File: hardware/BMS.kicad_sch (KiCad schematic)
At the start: 6 parts

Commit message: finished schematic except for 12v buck boost
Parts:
- added C69: 0.22u, Capacitor_SMD:C_0603_1608Metric_Pad1.08x0.95mm_HandSolder, symbol Device:C_Small
- added C70: 0.1u, Capacitor_SMD:C_0603_1608Metric_Pad1.08x0.95mm_HandSolder, symbol Device:C_Small
- added C71, C72, C73, C74, C75, C76: 100pF, Capacitor_SMD:C_0603_1608Metric_Pad1.08x0.95mm_HandSolder, symbol Device:C_Small
- added R107: 100k, Resistor_SMD:R_0603_1608Metric_Pad0.98x0.95mm_HandSolder, symbol Device:R_Small
- added R108: 10, Resistor_SMD:R_0603_1608Metric_Pad0.98x0.95mm_HandSolder, symbol Device:R_Small
- added R109, R110: 1k, Resistor_SMD:R_0603_1608Metric_Pad0.98x0.95mm_HandSolder, symbol Device:R_Small
- added R111, R112, R113, R114: 51, Resistor_SMD:R_0603_1608Metric_Pad0.98x0.95mm_HandSolder, symbol Device:R_Small
- added TR1, TR2: ADTT3-2, RF_Mini-Circuits:Mini-Circuits_CD636_H4.11mm, symbol Transformer:ADTT3-2
- added U13, U14: PESD5V0L2BT, LHRS_ICs:SOT23_NXP, symbol lhrs_misc:PESD5V0L2BT
- C67: renamed from C?; footprint (none) -> Capacitor_SMD:C_0603_1608Metric_Pad1.08x0.95mm_HandSolder
- C68: renamed from C?; value 0.1u -> 0.22u; footprint (none) -> Capacitor_SMD:C_0603_1608Metric_Pad1.08x0.95mm_HandSolder
- IC4: renamed from IC?; footprint SOP65P640X120-16N -> LHRS_ICs:SOP65P640X120-16N
- R104, R105, R106: renamed from R?; footprint (none) -> Resistor_SMD:R_0603_1608Metric_Pad0.98x0.95mm_HandSolder
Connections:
- net GND: now also C68.2, IC4.6 (SCLK), IC4.7 (NCS), IC4.8 (NUART/SPI_(SPI_RDY)), C69.2, C70.2, C71.2, C72.2, C73.2, C74.2, C75.1, C76.1, R107.2, U13.3, U14.3
- net INH: now also IC4.16 (INH), R107.1
- net at IC4.1 (DVDD): now also C68.1
- net COMLP: now reaches IC4.10 (COMLP)
- net COMLP: now also C71.1, R109.1, R111.1
- net COMLN: now reaches IC4.11 (COMLN)
- net COMLN: now also C72.1, R109.2, R112.1
- net COMHN: now reaches IC4.12 (COMHN)
- net COMHN: now also C74.1, R110.2, R114.1
- net COMHP: now reaches IC4.13 (COMHP)
- net COMHP: now also C73.1, R110.1, R113.1
- net at IC4.14 (CVDD): now also C69.1
- net at IC4.15 (BAT): now also C70.1, R108.1
- new net: C75.2, TR1.2
- new net: R111.2, TR2.3, U14.2
- new net: R114.2, TR1.1, U13.1
- new net: R113.2, TR1.3, U13.2
- new net: R112.2, TR2.1, U14.1
- new net: C76.2, TR2.2
- new net VBAT: R108.2
- new net isolatedCOMHN: TR1.6
- new net isolatedCOMHP: TR1.4
- new net isolatedCOMLN: TR2.6
- new net isolatedCOMLP: TR2.4
- no-connect marks 0 -> 2
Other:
- note added: "General Isolation"
- note added: "Transformer Isolation"
- moved on the sheet: C68, IC4

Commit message: added 12V buck boost
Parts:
- renumbered C67 to C68, C68 to C69, C69 to C70, C70 to C71, C71 to C72, C72 to C73, C73 to C74, C74 to C75, C75 to C76, C76 to C77, R104 to R108, R105 to R109, R106 to R110, R107 to R111, R108 to R112, R109 to R113, R110 to R114, R111 to R115, R112 to R116, R113 to R117, R114 to R118
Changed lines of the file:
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@@
 		(in_pos_files yes)
 		(dnp no)
-		(property "Reference" "C75"
+		(property "Reference" "C76"
 			(at 228.727 88.519 90)
 			(show_name no)
@@
 			(project "PS-BPSLeader"
 				(path "/d4a4ed4f-0983-4aef-b212-0e3284ab3963/e693f766-4bc7-4d67-a672-39e10f482b8b"
-					(reference "C75")
+					(reference "C76")
 					(unit 1)
 				)
@@
 		(dnp no)
 		(fields_autoplaced yes)
-		(property "Reference" "C67"
+		(property "Reference" "C68"
 			(at 22.86 27.9462 0)
 			(show_name no)
@@
 			(project "PS-BPSLeader"
 				(path "/d4a4ed4f-0983-4aef-b212-0e3284ab3963/e693f766-4bc7-4d67-a672-39e10f482b8b"
-					(reference "C67")
+					(reference "C68")
 					(unit 1)
 				)
@@
 		(dnp no)
 		(fields_autoplaced yes)
-		(property "Reference" "R111"
+		(property "Reference" "R115"
 			(at 189.23 118.11 90)
 			(show_name no)
@@
 			(project "PS-BPSLeader"
 				(path "/d4a4ed4f-0983-4aef-b212-0e3284ab3963/e693f766-4bc7-4d67-a672-39e10f482b8b"
-					(reference "R111")
+					(reference "R115")
 					(unit 1)
 				)
@@
 		(dnp no)
 		(fields_autoplaced yes)
-		(property "Reference" "R104"
+		(property "Reference" "R108"
 			(at 41.275 26.0349 0)
 			(show_name no)
@@
 			(project "PS-BPSLeader"
 				(path "/d4a4ed4f-0983-4aef-b212-0e3284ab3963/e693f766-4bc7-4d67-a672-39e10f482b8b"
-					(reference "R104")
+					(reference "R108")
 					(unit 1)
 				)
@@
 		(dnp no)
 		(fields_autoplaced yes)
-		(property "Reference" "C72"
+		(property "Reference" "C73"
 			(at 177.8 144.1512 0)
 			(show_name no)
@@
 			(project "PS-BPSLeader"
 				(path "/d4a4ed4f-0983-4aef-b212-0e3284ab3963/e693f766-4bc7-4d67-a672-39e10f482b8b"
-					(reference "C72")
+					(reference "C73")
 					(unit 1)
 				)
@@
 		(dnp no)
 		(fields_autoplaced yes)
-		(property "Reference" "C74"
+		(property "Reference" "C75"
 			(at 179.07 101.6062 0)
 			(show_name no)
@@
 			(project "PS-BPSLeader"
 				(path "/d4a4ed4f-0983-4aef-b212-0e3284ab3963/e693f766-4bc7-4d67-a672-39e10f482b8b"
-					(reference "C74")
+					(reference "C75")
 					(unit 1)
 				)
@@
 		(dnp no)
 		(fields_autoplaced yes)
-		(property "Reference" "R108"
+		(property "Reference" "R112"
 			(at 120.65 83.8199 0)
 			(show_name no)
@@
 			(project "PS-BPSLeader"
 				(path "/d4a4ed4f-0983-4aef-b212-0e3284ab3963/e693f766-4bc7-4d67-a672-39e10f482b8b"
-					(reference "R108")
+					(reference "R112")
 					(unit 1)
 				)
@@
 		(dnp no)
 		(fields_autoplaced yes)
-		(property "Reference" "C71"
+		(property "Reference" "C72"
 			(at 177.8 126.3712 0)
 			(show_name no)
@@
 			(project "PS-BPSLeader"
 				(path "/d4a4ed4f-0983-4aef-b212-0e3284ab3963/e693f766-4bc7-4d67-a672-39e10f482b8b"
-					(reference "C71")
+					(reference "C72")
 					(unit 1)
 				)
@@
 		(dnp no)
 		(fields_autoplaced yes)
-		(property "Reference" "C73"
+		(property "Reference" "C74"
 			(at 179.07 83.8262 0)
 			(show_name no)
@@
 			(project "PS-BPSLeader"
 				(path "/d4a4ed4f-0983-4aef-b212-0e3284ab3963/e693f766-4bc7-4d67-a672-39e10f482b8b"
-					(reference "C73")
+					(reference "C74")
 					(unit 1)
 				)
@@
 		(dnp no)
 		(fields_autoplaced yes)
-		(property "Reference" "R109"
+		(property "Reference" "R113"
 			(at 167.64 131.4449 0)
 			(show_name no)
@@
 			(project "PS-BPSLeader"
 				(path "/d4a4ed4f-0983-4aef-b212-0e3284ab3963/e693f766-4bc7-4d67-a672-39e10f482b8b"
-					(reference "R109")
+					(reference "R113")
 					(unit 1)
 				)
@@
 		(dnp no)
 		(fields_autoplaced yes)
-		(property "Reference" "C70"
+		(property "Reference" "C71"
 			(at 121.285 91.4462 0)
 			(show_name no)
@@
 			(project "PS-BPSLeader"
 				(path "/d4a4ed4f-0983-4aef-b212-0e3284ab3963/e693f766-4bc7-4d67-a672-39e10f482b8b"
-					(reference "C70")
+					(reference "C71")
 					(unit 1)
 				)
@@
 		(dnp no)
 		(fields_autoplaced yes)
-		(property "Reference" "R106"
+		(property "Reference" "R110"
 			(at 60.96 26.0349 0)
 			(show_name no)
@@
 			(project "PS-BPSLeader"
 				(path "/d4a4ed4f-0983-4aef-b212-0e3284ab3963/e693f766-4bc7-4d67-a672-39e10f482b8b"
-					(reference "R106")
+					(reference "R110")
 					(unit 1)
 				)
@@
 		(dnp no)
 		(fields_autoplaced yes)
-		(property "Reference" "R114"
+		(property "Reference" "R118"
 			(at 189.865 93.98 90)
 			(show_name no)
@@
 			(project "PS-BPSLeader"
 				(path "/d4a4ed4f-0983-4aef-b212-0e3284ab3963/e693f766-4bc7-4d67-a672-39e10f482b8b"
-					(reference "R114")
+					(reference "R118")
 					(unit 1)
 				)
@@
 		(in_pos_files yes)
 		(dnp no)
-		(property "Reference" "C76"
+		(property "Reference" "C77"
 			(at 229.362 131.064 90)
 			(show_name no)
@@
 			(project "PS-BPSLeader"
 				(path "/d4a4ed4f-0983-4aef-b212-0e3284ab3963/e693f766-4bc7-4d67-a672-39e10f482b8b"
-					(reference "C76")
+					(reference "C77")
 					(unit 1)
 				)
@@
 		(dnp no)
 		(fields_autoplaced yes)
-		(property "Reference" "R113"
+		(property "Reference" "R117"
 			(at 189.865 76.2 90)
 			(show_name no)
@@
 			(project "PS-BPSLeader"
 				(path "/d4a4ed4f-0983-4aef-b212-0e3284ab3963/e693f766-4bc7-4d67-a672-39e10f482b8b"
-					(reference "R113")
+					(reference "R117")
 					(unit 1)
 				)
@@
 		(dnp no)
 		(fields_autoplaced yes)
-		(property "Reference" "R110"
+		(property "Reference" "R114"
 			(at 168.275 88.8999 0)
 			(show_name no)
@@
 			(project "PS-BPSLeader"
 				(path "/d4a4ed4f-0983-4aef-b212-0e3284ab3963/e693f766-4bc7-4d67-a672-39e10f482b8b"
-					(reference "R110")
+					(reference "R114")
 					(unit 1)
 				)
@@
 		(dnp no)
 		(fields_autoplaced yes)
-		(property "Reference" "C68"
+		(property "Reference" "C69"
 			(at 47.625 114.9412 0)
 			(show_name no)
@@
 			(project "PS-BPSLeader"
 				(path "/d4a4ed4f-0983-4aef-b212-0e3284ab3963/e693f766-4bc7-4d67-a672-39e10f482b8b"
-					(reference "C68")
+					(reference "C69")
 					(unit 1)
 				)
@@
 		(dnp no)
 		(fields_autoplaced yes)
-		(property "Reference" "R107"
+		(property "Reference" "R111"
 			(at 80.645 25.3999 0)
 			(show_name no)
@@
 			(project "PS-BPSLeader"
 				(path "/d4a4ed4f-0983-4aef-b212-0e3284ab3963/e693f766-4bc7-4d67-a672-39e10f482b8b"
-					(reference "R107")
+					(reference "R111")
 					(unit 1)
 				)
@@
 		(dnp no)
 		(fields_autoplaced yes)
-		(property "Reference" "R112"
+		(property "Reference" "R116"
 			(at 189.23 135.89 90)
 			(show_name no)
@@
 			(project "PS-BPSLeader"
 				(path "/d4a4ed4f-0983-4aef-b212-0e3284ab3963/e693f766-4bc7-4d67-a672-39e10f482b8b"
-					(reference "R112")
+					(reference "R116")
 					(unit 1)
 				)
@@
 		(dnp no)
 		(fields_autoplaced yes)
-		(property "Reference" "C69"
+		(property "Reference" "C70"
 			(at 108.585 92.7162 0)
 			(show_name no)
@@
 			(project "PS-BPSLeader"
 				(path "/d4a4ed4f-0983-4aef-b212-0e3284ab3963/e693f766-4bc7-4d67-a672-39e10f482b8b"
-					(reference "C69")
+					(reference "C70")
 					(unit 1)
 				)
@@
 		(dnp no)
 		(fields_autoplaced yes)
-		(property "Reference" "R105"
+		(property "Reference" "R109"
 			(at 51.435 26.0349 0)
 			(show_name no)
@@
 			(project "PS-BPSLeader"
 				(path "/d4a4ed4f-0983-4aef-b212-0e3284ab3963/e693f766-4bc7-4d67-a672-39e10f482b8b"
-					(reference "R105")
-					(unit 1)
-				)
+					(reference "R109")
+					(unit 1)
+				)

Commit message: forgot to push last night
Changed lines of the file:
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@@
 	)
 	(hierarchical_label "MOSI{slash}RX"
-		(shape input)
+		(shape bidirectional)
 		(at 38.735 32.385 270)
 		(effects
@@
 	)
 	(hierarchical_label "MOSI{slash}RX"
-		(shape input)
+		(shape bidirectional)
 		(at 40.005 91.44 180)
 		(effects
@@
 	)
 	(hierarchical_label "MISO{slash}TX"
-		(shape input)
+		(shape bidirectional)
 		(at 48.895 32.385 270)
 		(effects

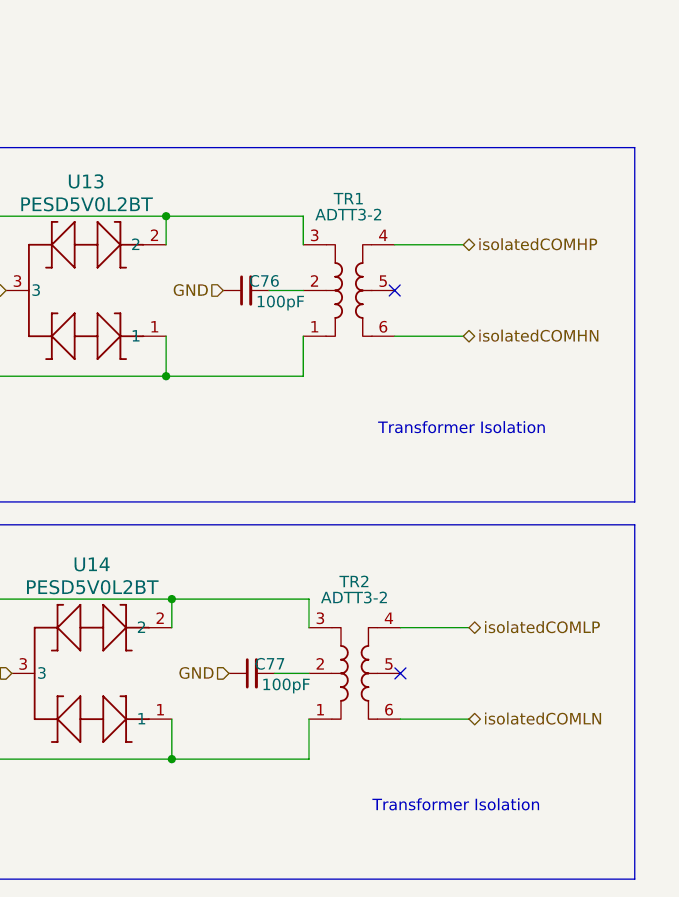
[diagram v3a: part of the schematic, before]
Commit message: kms drc crashed and didn't save layout
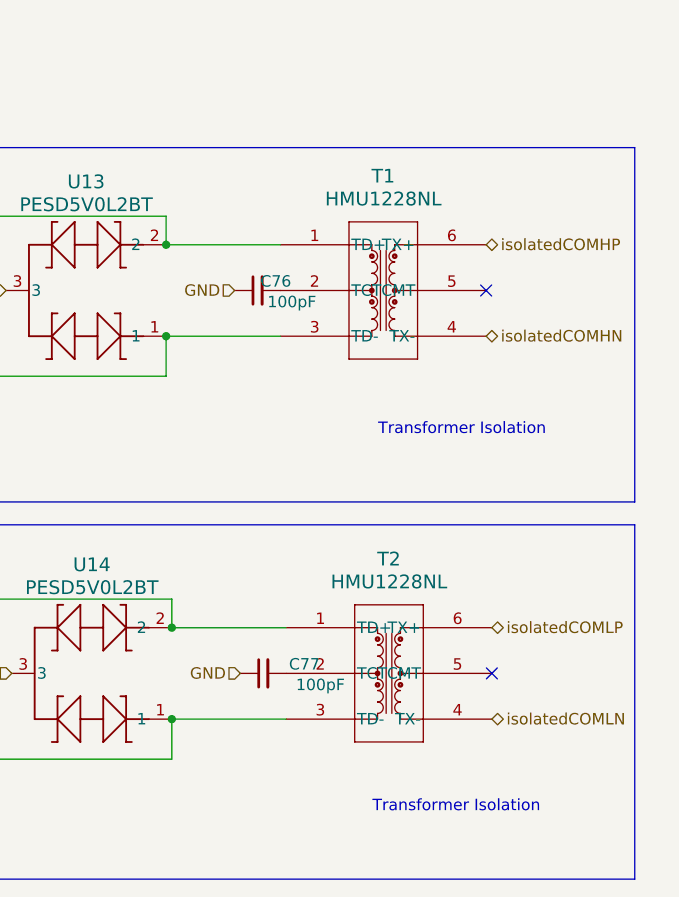
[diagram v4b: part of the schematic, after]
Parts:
- removed TR1, TR2: ADTT3-2, RF_Mini-Circuits:Mini-Circuits_CD636_H4.11mm, symbol Transformer:ADTT3-2
- added T1, T2: HMU1228NL, LHRS_Special:HMU1228NL_PUL, symbol lhrs_special:HMU1228NL
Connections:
- net isolatedCOMHN: now also T1.4 (TX-)
- net isolatedCOMHP: now also T1.6 (TX+)
- net isolatedCOMLN: now also T2.4 (TX-)
- net isolatedCOMLP: now also T2.6 (TX+)
- net at C76.2: now also T1.2 (TCT)
- net at R115.2, U14.2: now also T2.1 (TD+)
- net at R118.2, U13.1: now also T1.3 (TD-)
- net at R117.2, U13.2: now also T1.1 (TD+)
- net at R116.2, U14.1: now also T2.3 (TD-)
- net at C77.2: now also T2.2 (TCT)
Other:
- moved on the sheet: C76, C77

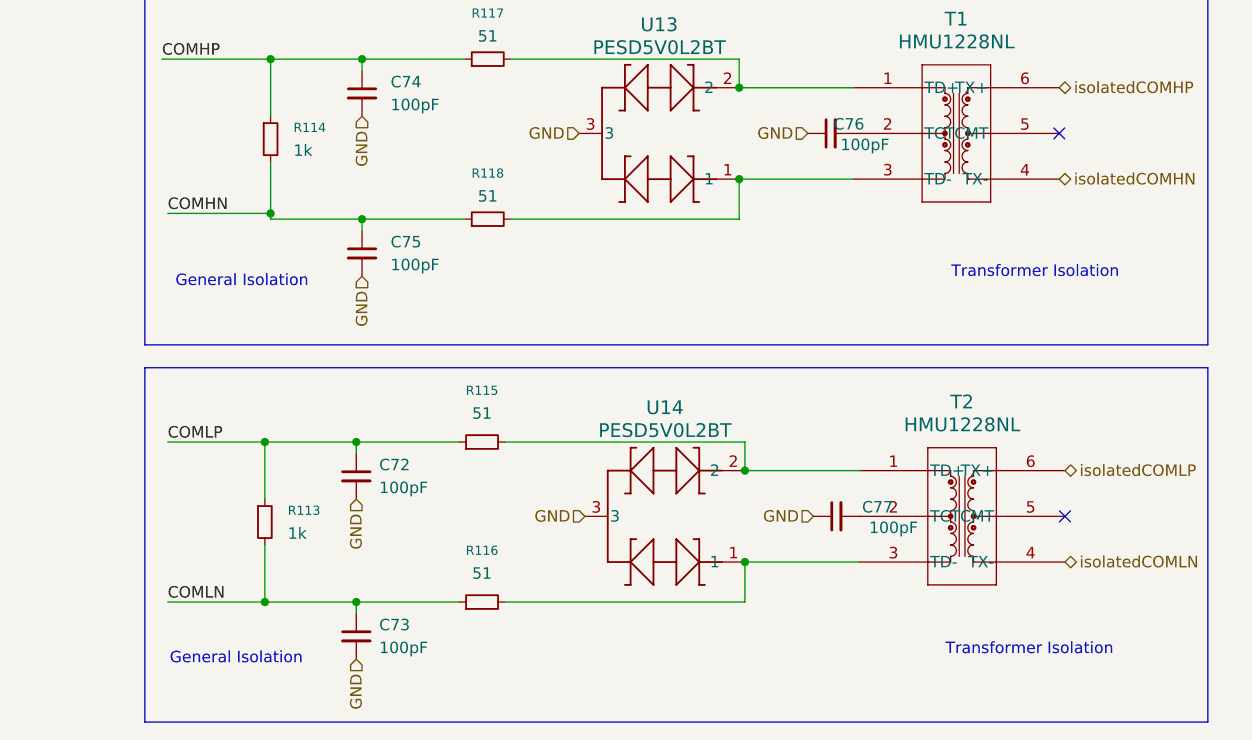
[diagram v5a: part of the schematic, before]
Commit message: chopped but passes DRC
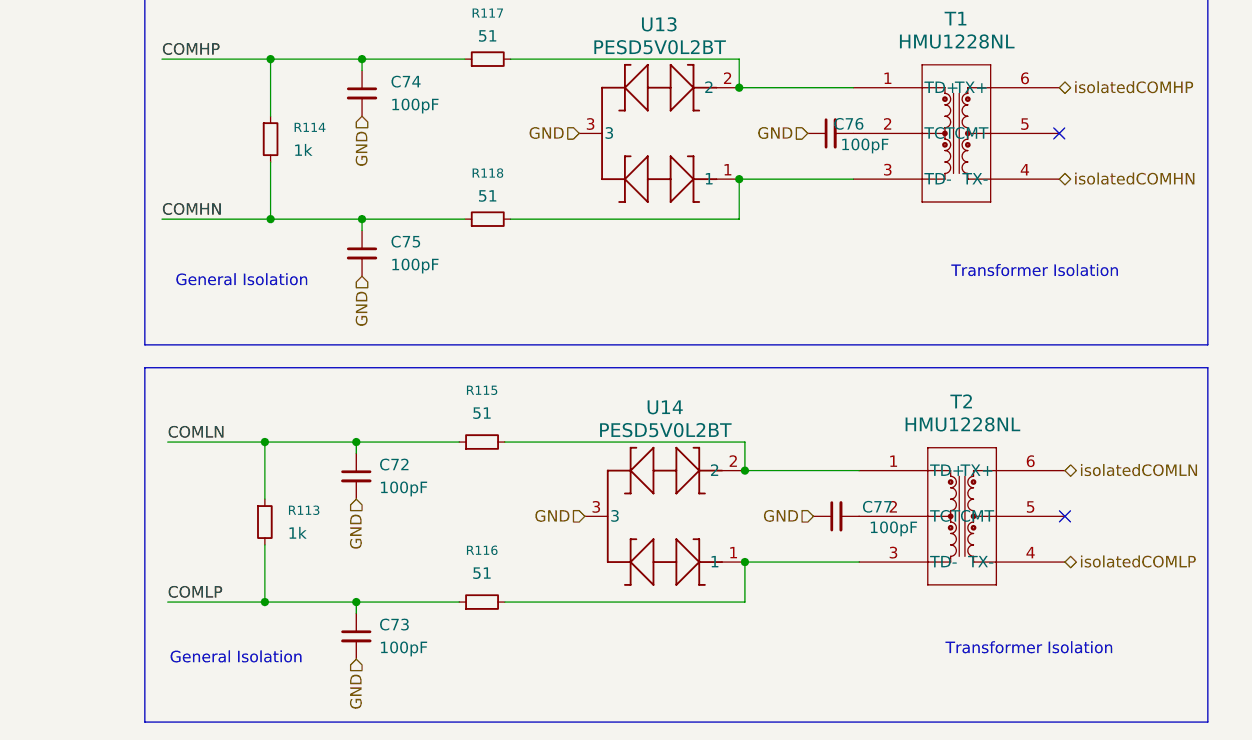
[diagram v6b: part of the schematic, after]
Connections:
- net COMLN: now also C72.1, R113.1, R115.1; no longer C73.1, R113.2, R116.1
- net COMLP: now also C73.1, R113.2, R116.1; no longer C72.1, R113.1, R115.1
- net isolatedCOMLN: now also T2.6 (TX+); no longer T2.4 (TX-)
- net isolatedCOMLP: now also T2.4 (TX-); no longer T2.6 (TX+)
